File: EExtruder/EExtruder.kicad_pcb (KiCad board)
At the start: 2 copper layers, 73.4 x 47.1 mm, 97 parts, among them J1 20A 50V, J11 Conn_01x03_Male, J2 AudioJack4, J3 6A 50V, J4 6A 50V, J5 Conn_01x02, J6 Conn_01x02, J7 Conn_01x03_Male, J8 Conn_01x03_Male, J9 Conn_01x03_Male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

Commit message: Updated EExtruder board rev.
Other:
- board text added: "EExtruder rev4"
- board text removed: "EExtruder rev3"
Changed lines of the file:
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@@
   )
   (setup
-    (last_trace_width 0.762)
+    (last_trace_width 0.1524)
     (user_trace_width 0.1524)
     (user_trace_width 0.3048)
@@
     (effects (font (size 1.5 1.5) (thickness 0.3)) (justify mirror))
   )
-  (gr_text "EExtruder\nrev3" (at 192.1 92.9) (layer B.SilkS)
+  (gr_text "EExtruder\nrev4" (at 192.1 92.9) (layer B.SilkS)
     (effects (font (size 1.5 1.5) (thickness 0.3)) (justify mirror))
   )

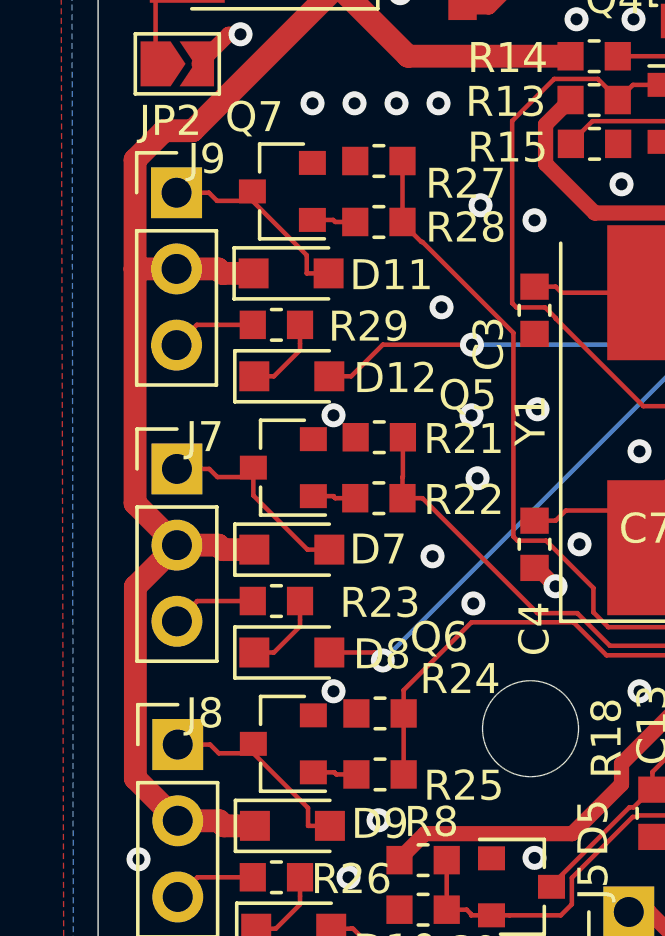
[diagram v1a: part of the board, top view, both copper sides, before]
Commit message: Updated traces for fan connectors.
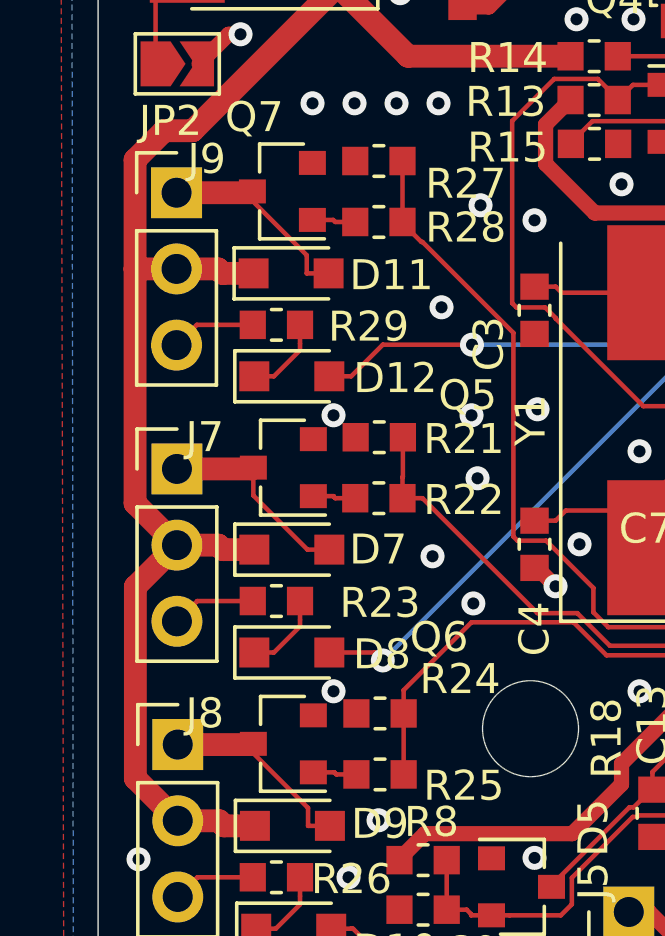
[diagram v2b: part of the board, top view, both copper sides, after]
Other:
- board text added: "EExtruder rev 4"
- board text removed: "EExtruder rev4"
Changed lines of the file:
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@@
-(kicad_pcb (version 20171130) (host pcbnew 6.0.0-rc1-unknown-170ff66~66~ubuntu18.10.1)
+(kicad_pcb (version 20171130) (host pcbnew 6.0.0-rc1-unknown-ff9d814~66~ubuntu18.10.1)
   (general
     (thickness 1.6)
     (drawings 59)
-    (tracks 1179)
+    (tracks 1176)
     (zones 0)
     (modules 97)
@@
   )
   (setup
-    (last_trace_width 0.1524)
+    (last_trace_width 0.762)
     (user_trace_width 0.1524)
     (user_trace_width 0.3048)
@@
     (effects (font (size 1.5 1.5) (thickness 0.3)) (justify mirror))
   )
-  (gr_text "EExtruder\nrev4" (at 192.1 92.9) (layer B.SilkS)
+  (gr_text "EExtruder\nrev 4" (at 192.1 92.9) (layer B.SilkS)
     (effects (font (size 1.5 1.5) (thickness 0.3)) (justify mirror))
   )
@@
   (segment (start 134.9311 116.078) (end 133.128 114.2749) (width 0.1524) (layer F.Cu) (net 16))
   (segment (start 133.128 114.2749) (end 133.128 113.6594) (width 0.1524) (layer F.Cu) (net 16))
-  (segment (start 133.128 113.6594) (end 131.9303 113.6594) (width 0.1524) (layer F.Cu) (net 16))
-  (segment (start 131.9303 113.6594) (end 131.6589 113.388) (width 0.1524) (layer F.Cu) (net 16))
   (segment (start 135.66 116.078) (end 134.9311 116.078) (width 0.1524) (layer F.Cu) (net 16))
-  (segment (start 130.58 113.388) (end 131.6589 113.388) (width 0.1524) (layer F.Cu) (net 16))
   (segment (start 133.128 113.345) (end 133.128 113.6594) (width 0.1524) (layer F.Cu) (net 16))
+  (segment (start 133.085 113.388) (end 133.128 113.345) (width 0.762) (layer F.Cu) (net 16))
+  (segment (start 130.58 113.388) (end 133.085 113.388) (width 0.762) (layer F.Cu) (net 16))
   (segment (start 160.873 108.426) (end 160.873 109.3049) (width 0.1524) (layer F.Cu) (net 17))
   (segment (start 155.6095 109.9427) (end 156.224 110.5572) (width 0.1524) (layer F.Cu) (net 17))
@@
   (segment (start 133.16 119.507) (end 133.8124 119.507) (width 0.1524) (layer F.Cu) (net 18))
   (segment (start 135.68 125.286) (end 134.9511 125.286) (width 0.1524) (layer F.Cu) (net 19))
-  (segment (start 133.128 122.8664) (end 131.9763 122.8664) (width 0.1524) (layer F.Cu) (net 19))
-  (segment (start 131.9763 122.8664) (end 131.6859 122.576) (width 0.1524) (layer F.Cu) (net 19))
   (segment (start 134.9511 125.286) (end 134.9511 124.6895) (width 0.1524) (layer F.Cu) (net 19))
   (segment (start 134.9511 124.6895) (end 133.128 122.8664) (width 0.1524) (layer F.Cu) (net 19))
-  (segment (start 130.607 122.576) (end 131.6859 122.576) (width 0.1524) (layer F.Cu) (net 19))
   (segment (start 133.128 122.552) (end 133.128 122.8664) (width 0.1524) (layer F.Cu) (net 19))
+  (segment (start 133.104 122.576) (end 133.128 122.552) (width 0.762) (layer F.Cu) (net 19))
+  (segment (start 130.607 122.576) (end 133.104 122.576) (width 0.762) (layer F.Cu) (net 19))
   (segment (start 160.373 107.5471) (end 161.668 107.5471) (width 0.1524) (layer F.Cu) (net 20))
   (segment (start 161.668 107.5471) (end 162.1513 108.0304) (width 0.1524) (layer F.Cu) (net 20))
@@
   (segment (start 133.223 128.714) (end 133.8754 128.714) (width 0.1524) (layer F.Cu) (net 21))
   (segment (start 135.636 106.87) (end 134.9071 106.87) (width 0.1524) (layer F.Cu) (net 22))
-  (segment (start 133.096 104.4524) (end 131.9183 104.4524) (width 0.1524) (layer F.Cu) (net 22))
-  (segment (start 131.9183 104.4524) (end 131.6469 104.181) (width 0.1524) (layer F.Cu) (net 22))
   (segment (start 134.9071 106.87) (end 134.9071 106.2635) (width 0.1524) (layer F.Cu) (net 22))
   (segment (start 134.9071 106.2635) (end 133.096 104.4524) (width 0.1524) (layer F.Cu) (net 22))
-  (segment (start 130.568 104.181) (end 131.6469 104.181) (width 0.1524) (layer F.Cu) (net 22))
   (segment (start 133.096 104.138) (end 133.096 104.4524) (width 0.1524) (layer F.Cu) (net 22))
+  (segment (start 133.053 104.181) (end 133.096 104.138) (width 0.762) (layer F.Cu) (net 22))
+  (segment (start 130.568 104.181) (end 133.053 104.181) (width 0.762) (layer F.Cu) (net 22))
   (segment (start 160.7548 114.739) (end 160.7548 114.6113) (width 0.1524) (layer B.Cu) (net 23))
   (segment (start 160.7548 114.6113) (end 157.4541 111.3106) (width 0.1524) (layer B.Cu) (net 23))

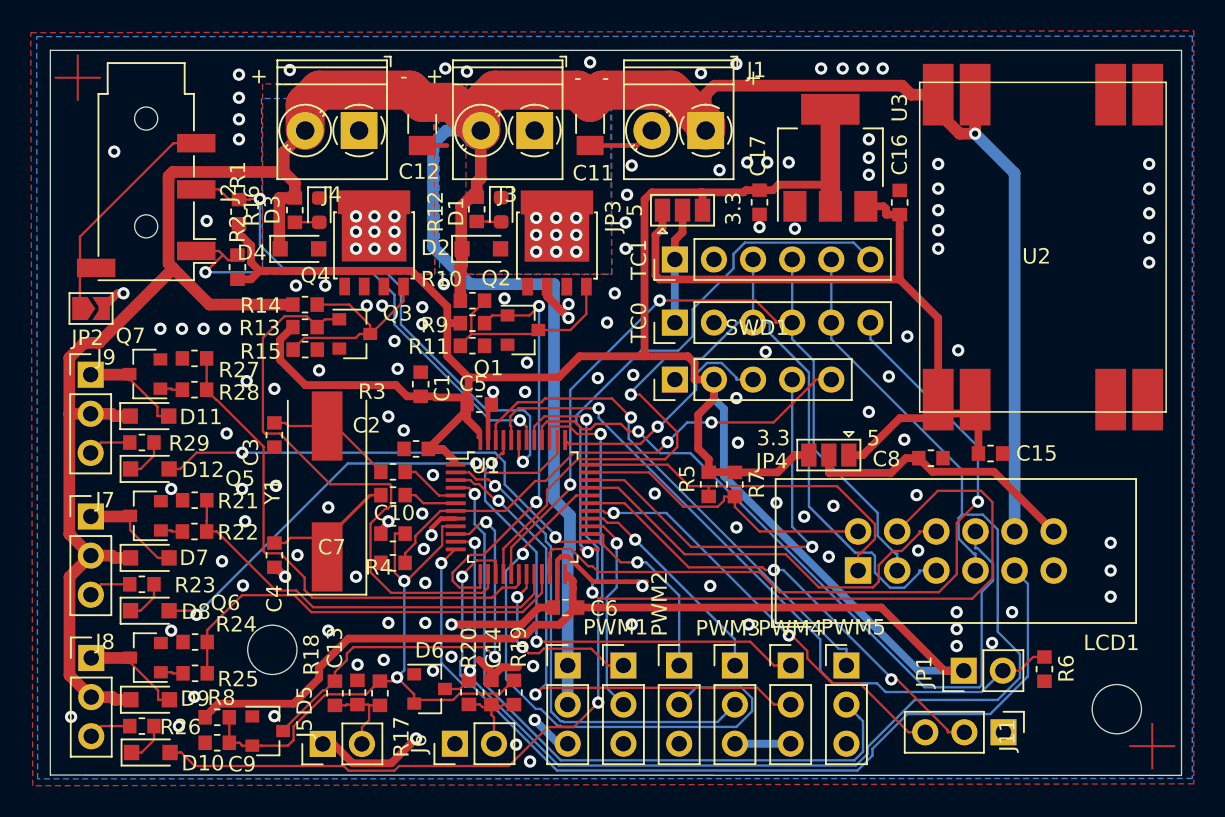
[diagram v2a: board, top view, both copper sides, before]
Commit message: Added voltage selector for the fans.
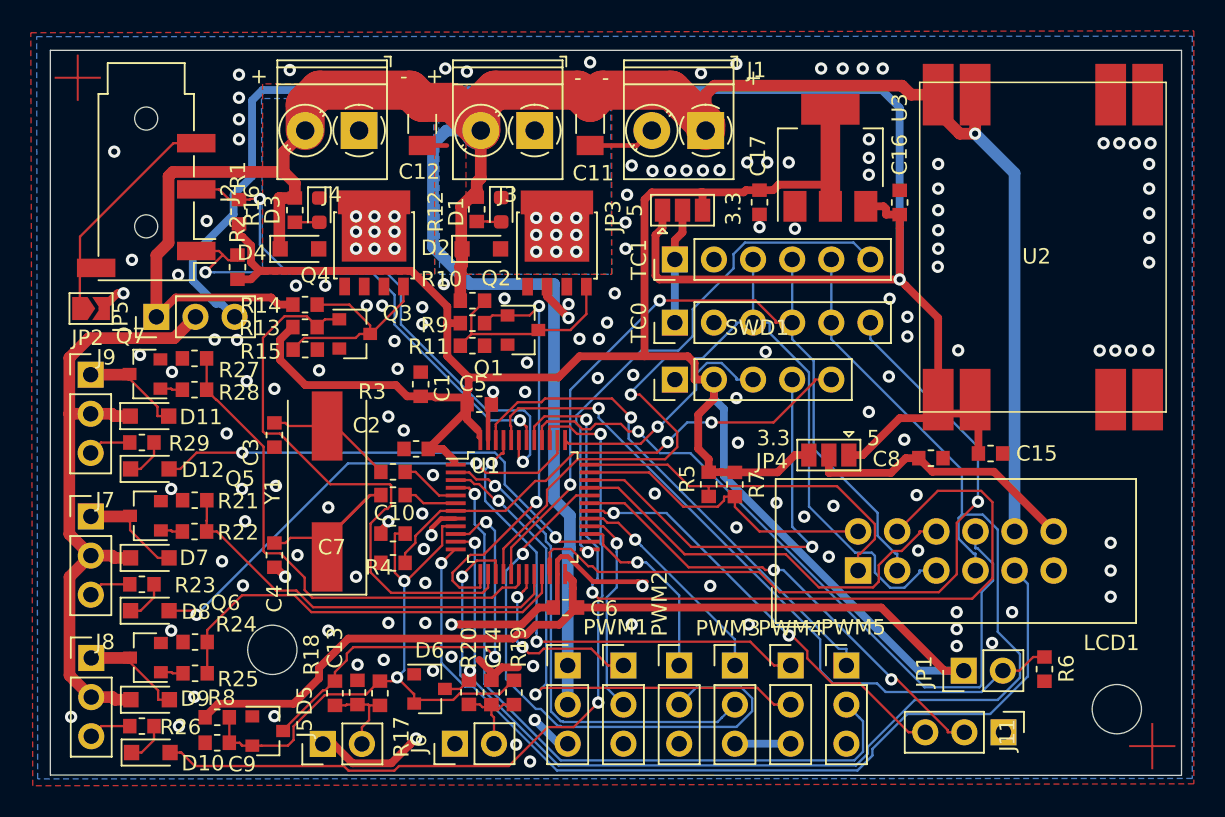
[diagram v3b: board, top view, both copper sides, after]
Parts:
- added JP5: Fan Power Select, Connector_PinHeader_2.54mm:PinHeader_1x03_P2.54mm_Vertical, F.Cu at (134.8, 100.4)
- JP3: value Jumper_3_Open -> TC Power Select
- JP4: value Jumper_3_Open -> LCD Power Select
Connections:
- D11 pad 1: /VIN -> /Vfan
- D7 pad 1: /VIN -> /Vfan
- D9 pad 1: /VIN -> /Vfan
- J7 pad 2: /VIN -> /Vfan
- J8 pad 2: /VIN -> /Vfan
- J9 pad 2: /VIN -> /Vfan
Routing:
- net /5V: track 50.1 -> 121.0 mm, vias 0 -> 1
- net /Vfan: track 0.00 -> 42.4 mm
- net /VIN: track 219.3 -> 181.2 mm
- net GND: vias 131 -> 150

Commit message: Add round edges.
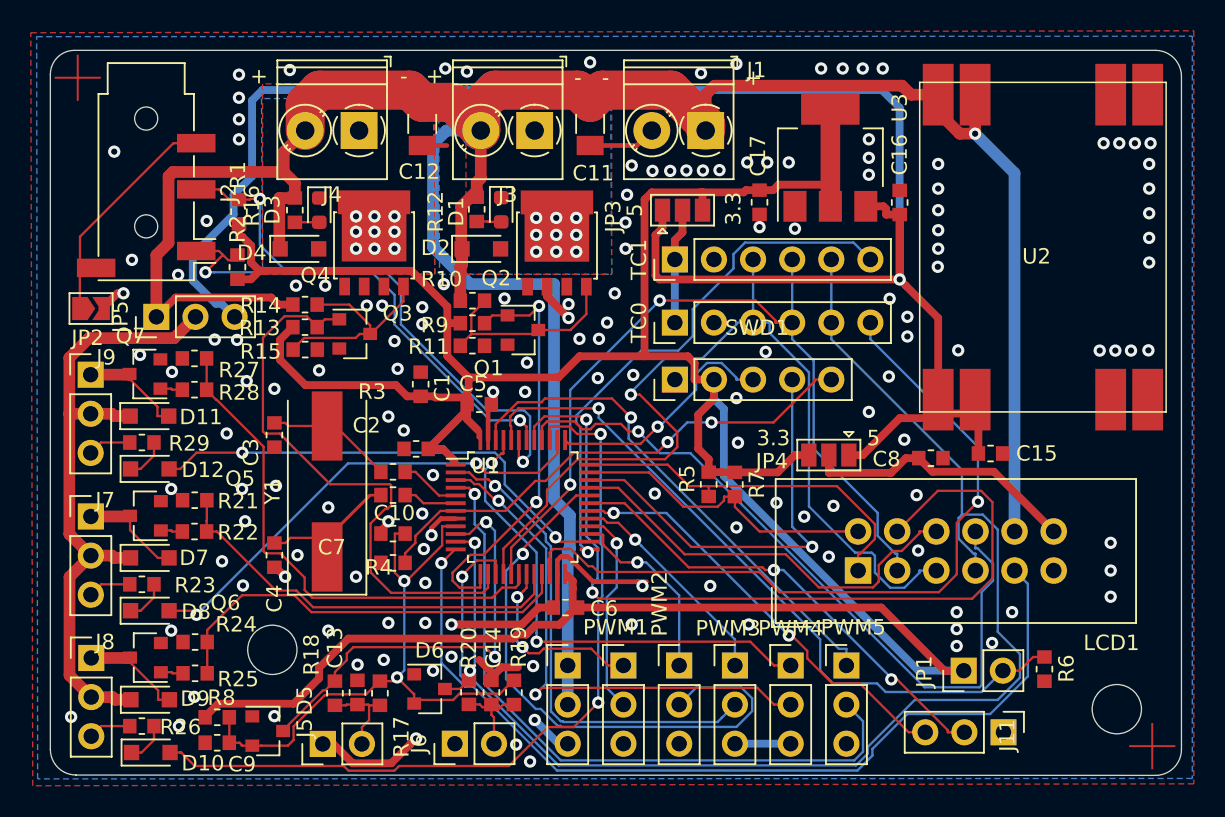
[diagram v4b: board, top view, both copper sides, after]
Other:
- outline, holes or cut-outs redrawn
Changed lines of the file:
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@@
   (general
     (thickness 1.6)
-    (drawings 59)
+    (drawings 63)
     (tracks 1212)
     (zones 0)
@@
   )
   (setup
-    (last_trace_width 0.508)
+    (last_trace_width 0.1524)
     (user_trace_width 0.1524)
     (user_trace_width 0.3048)
@@
     )
   )
+  (gr_arc (start 129.6162 128.5113) (end 127.9525 128.5113) (angle -90) (layer Edge.Cuts) (width 0.05))
+  (gr_arc (start 199.7075 84.8106) (end 201.3966 84.8106) (angle -90) (layer Edge.Cuts) (width 0.05))
+  (gr_arc (start 199.7075 128.5113) (end 199.7075 130.2004) (angle -90) (layer Edge.Cuts) (width 0.05))
+  (gr_arc (start 129.5146 84.6836) (end 129.5146 83.1215) (angle -90) (layer Edge.Cuts) (width 0.05))
   (gr_text - (at 162.2 84.9) (layer F.SilkS)
     (effects (font (size 1 1) (thickness 0.15)))
@@
     (effects (font (size 1 1) (thickness 0.15)) (justify mirror))
   )
-  (gr_line (start 127.9525 130.175) (end 127.9525 83.1215) (layer Edge.Cuts) (width 0.05))
-  (gr_line (start 201.4 130.2) (end 127.9525 130.175) (layer Edge.Cuts) (width 0.05))
-  (gr_line (start 201.4 83.1215) (end 201.4 130.175) (layer Edge.Cuts) (width 0.05))
-  (gr_line (start 127.9525 83.1215) (end 201.4 83.1215) (layer Edge.Cuts) (width 0.05))
+  (gr_line (start 127.9525 128.5113) (end 127.9525 84.6836) (layer Edge.Cuts) (width 0.05))
+  (gr_line (start 199.7075 130.2004) (end 129.6162 130.175) (layer Edge.Cuts) (width 0.05))
+  (gr_line (start 201.3966 84.8106) (end 201.3966 128.5113) (layer Edge.Cuts) (width 0.05))
+  (gr_line (start 129.5273 83.1215) (end 199.7075 83.1215) (layer Edge.Cuts) (width 0.05))
   (segment (start 153.3182 113.526) (end 152.704545 114.139655) (width 0.3048) (layer F.Cu) (net 1))
   (segment (start 154.273 113.526) (end 153.3182 113.526) (width 0.3048) (layer F.Cu) (net 1))
@@
   (segment (start 149.3145 124.0785) (end 148.455601 124.937399) (width 0.1524) (layer F.Cu) (net 6))
   (segment (start 149.352 124.0785) (end 149.3145 124.0785) (width 0.1524) (layer F.Cu) (net 6))
-  (segment (start 130.58 115.928) (end 129.1949 117.3131) (width 0.762) (layer F.Cu) (net 72))
-  (segment (start 129.1949 117.3131) (end 129.1949 123.7039) (width 0.762) (layer F.Cu) (net 72))
-  (segment (start 129.1949 123.7039) (end 130.607 125.116) (width 0.762) (layer F.Cu) (net 72))
-  (segment (start 129.1843 106.721) (end 129.1843 114.5323) (width 0.762) (layer F.Cu) (net 72))
-  (segment (start 129.1843 114.5323) (end 130.58 115.928) (width 0.762) (layer F.Cu) (net 72))
-  (segment (start 129.1843 106.721) (end 129.1843 103.0858) (width 0.762) (layer F.Cu) (net 72))
-  (segment (start 130.568 106.721) (end 129.1843 106.721) (width 0.762) (layer F.Cu) (net 72))
   (segment (start 143.1054 91.0162) (end 135.9081 91.0162) (width 0.762) (layer F.Cu) (net 7))
   (segment (start 135.9081 91.0162) (end 135.6274 91.2969) (width 0.762) (layer F.Cu) (net 7))
-  (segment (start 130.5913 106.721) (end 130.568 106.721) (width 0.762) (layer F.Cu) (net 72))
-  (segment (start 130.5913 106.721) (end 130.6145 106.721) (width 0.762) (layer F.Cu) (net 72))
   (segment (start 143.828 91.7388) (end 143.1054 91.0162) (width 0.762) (layer F.Cu) (net 7))
   (segment (start 143.1054 91.0162) (end 143.1054 89.7231) (width 0.762) (layer F.Cu) (net 7))
@@
   (segment (start 155.638 91.6878) (end 155.9 91.4258) (width 0.762) (layer F.Cu) (net 7))
   (segment (start 155.9 91.4258) (end 155.9 88.3285) (width 0.762) (layer F.Cu) (net 7))
-  (segment (start 132.1023 106.87) (end 131.9533 106.721) (width 0.762) (layer F.Cu) (net 72))
-  (segment (start 131.9533 106.721) (end 130.6145 106.721) (width 0.762) (layer F.Cu) (net 72))
-  (segment (start 133.136 106.87) (end 132.1023 106.87) (width 0.762) (layer F.Cu) (net 72))
   (segment (start 155.638 92.2539) (end 155.638 91.6878) (width 0.762) (layer F.Cu) (net 7))
   (segment (start 155.638 92.659) (end 155.638 92.2539) (width 0.762) (layer F.Cu) (net 7))
@@
   (segment (start 154.686 96.012) (end 154.686 96.5203) (width 0.762) (layer F.Cu) (net 7))
   (segment (start 188 86) (end 188 88.5337) (width 0.762) (layer F.Cu) (net 7))
-  (segment (start 133.18 125.286) (end 132.1463 125.286) (width 0.762) (layer F.Cu) (net 72))
-  (segment (start 130.607 125.116) (end 131.9907 125.116) (width 0.762) (layer F.Cu) (net 72))
-  (segment (start 132.1463 125.286) (end 132.1463 125.2716) (width 0.762) (layer F.Cu) (net 72))
-  (segment (start 132.1463 125.2716) (end 131.9907 125.116) (width 0.762) (layer F.Cu) (net 72))
-  (segment (start 130.58 115.928) (end 131.9637 115.928) (width 0.762) (layer F.Cu) (net 72))
-  (segment (start 133.16 116.078) (end 132.1137 116.078) (width 0.762) (layer F.Cu) (net 72))
-  (segment (start 132.1137 116.078) (end 131.9637 115.928) (width 0.762) (layer F.Cu) (net 72))
   (segment (start 154.686 97.0457) (end 154.5715 97.1602) (width 0.762) (layer F.Cu) (net 7))
   (segment (start 154.5715 97.1602) (end 154.5715 99.3775) (width 0.762) (layer F.Cu) (net 7))
@@
   (segment (start 169 94.9433) (end 168.5 95.4433) (width 0.508) (layer F.Cu) (net 71))
   (segment (start 168.5 100.8) (end 168.5 96.7) (width 0.508) (layer B.Cu) (net 71))
+  (segment (start 130.58 115.928) (end 129.1949 117.3131) (width 0.762) (layer F.Cu) (net 72))
+  (segment (start 129.1949 117.3131) (end 129.1949 123.7039) (width 0.762) (layer F.Cu) (net 72))
+  (segment (start 129.1949 123.7039) (end 130.607 125.116) (width 0.762) (layer F.Cu) (net 72))
+  (segment (start 129.1843 106.721) (end 129.1843 114.5323) (width 0.762) (layer F.Cu) (net 72))
+  (segment (start 129.1843 114.5323) (end 130.58 115.928) (width 0.762) (layer F.Cu) (net 72))
+  (segment (start 129.1843 106.721) (end 129.1843 103.0858) (width 0.762) (layer F.Cu) (net 72))
+  (segment (start 130.568 106.721) (end 129.1843 106.721) (width 0.762) (layer F.Cu) (net 72))
+  (segment (start 130.5913 106.721) (end 130.568 106.721) (width 0.762) (layer F.Cu) (net 72))
+  (segment (start 130.5913 106.721) (end 130.6145 106.721) (width 0.762) (layer F.Cu) (net 72))
+  (segment (start 132.1023 106.87) (end 131.9533 106.721) (width 0.762) (layer F.Cu) (net 72))
+  (segment (start 131.9533 106.721) (end 130.6145 106.721) (width 0.762) (layer F.Cu) (net 72))
+  (segment (start 133.136 106.87) (end 132.1023 106.87) (width 0.762) (layer F.Cu) (net 72))
+  (segment (start 133.18 125.286) (end 132.1463 125.286) (width 0.762) (layer F.Cu) (net 72))
+  (segment (start 130.607 125.116) (end 131.9907 125.116) (width 0.762) (layer F.Cu) (net 72))
+  (segment (start 132.1463 125.286) (end 132.1463 125.2716) (width 0.762) (layer F.Cu) (net 72))
+  (segment (start 132.1463 125.2716) (end 131.9907 125.116) (width 0.762) (layer F.Cu) (net 72))
+  (segment (start 130.58 115.928) (end 131.9637 115.928) (width 0.762) (layer F.Cu) (net 72))
+  (segment (start 133.16 116.078) (end 132.1137 116.078) (width 0.762) (layer F.Cu) (net 72))
+  (segment (start 132.1137 116.078) (end 131.9637 115.928) (width 0.762) (layer F.Cu) (net 72))
   (segment (start 130.461699 101.808401) (end 129.1843 103.0858) (width 0.762) (layer F.Cu) (net 72))
   (segment (start 137.375 100.425) (end 135.991599 101.808401) (width 0.762) (layer F.Cu) (net 72))
